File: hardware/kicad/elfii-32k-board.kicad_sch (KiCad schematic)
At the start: 15 parts, among them J1 ELFII_P3_86, U1 74HCT273, U2 62256, U3 74HCT04, U4 74HCT86, U5 74HCT32

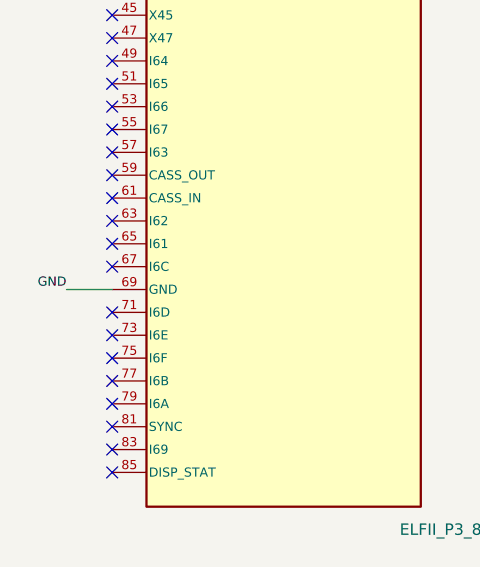
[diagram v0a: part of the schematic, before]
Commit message: Leave original-bus contact 69 NC pending GND discrepancy resolution
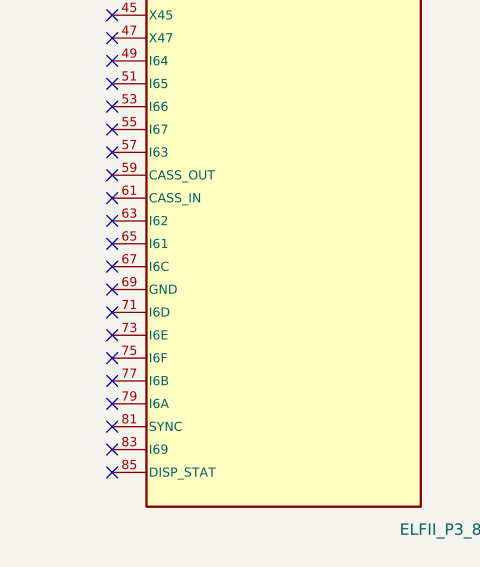
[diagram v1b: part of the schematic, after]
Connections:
- net GND: no longer J1.69 (GND)
- no-connect marks 70 -> 71
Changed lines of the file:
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@@
 (wire (pts (xy 56.950 243.740) (xy 51.870 243.740)) (stroke (width 0) (type default)))
 (label "GND" (at 51.870 243.740 0) (effects (font (size 1.016 1.016)) (justify right bottom)))
-(wire (pts (xy 56.950 325.020) (xy 51.870 325.020)) (stroke (width 0) (type default)))
-(label "GND" (at 51.870 325.020 0) (effects (font (size 1.016 1.016)) (justify right bottom)))
 (text "PROTOTYPE - NOT FABRICATION READY" (at 175 24 0) (effects (font (size 1.5 1.5)) (justify left)))
 (text "Original Netronics ELF II expansion bus - 86 contacts" (at 175 32 0) (effects (font (size 1.5 1.5)) (justify left)))
@@
 (no_connect (at 56.950 342.800))
 (no_connect (at 56.950 345.340))
+(no_connect (at 56.950 325.020))
 (sheet_instances (path "/" (page "1")))
 )

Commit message: Add functional schematic sections and explicit latch/decode annotations
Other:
- note added: "/CE = XOR(A15,REGION) OR NOT(ENABLE)"
- note added: "/OE = /CE OR /MRD /WE = /CE OR /MWR"
- note added: "32K STATIC RAM / U2"
- note added: "A0-A7: use MA0-MA7 during the memory phase"
- note added: "A8-A15: capture MA0-MA7 at TPA falling edge"
- note added: "CONTROL / 1802 CYCLES"
- note added: "EXPANSION BUS / J1"
- note added: "HIGH ADDRESS LATCH / U1"
- note added: "IMPORTANT: J1 pins 69 and 82 are disputed; remain NC."
- note added: "POWER BYPASS"
- note added: "REGION SELECT AND ENABLE"
- note added: "Schematic nets intentionally use short stubs and named labels."
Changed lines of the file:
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@@
 (no_connect (at 56.950 345.340))
 (no_connect (at 56.950 325.020))
+(text "EXPANSION BUS / J1" (at 41 40 0) (effects (font (size 1.8 1.8) (thickness 0.3)) (justify left)))
+(text "HIGH ADDRESS LATCH / U1" (at 175 75 0) (effects (font (size 1.8 1.8) (thickness 0.3)) (justify left)))
+(text "32K STATIC RAM / U2" (at 302 75 0) (effects (font (size 1.8 1.8) (thickness 0.3)) (justify left)))
+(text "CONTROL / 1802 CYCLES" (at 176 222 0) (effects (font (size 1.8 1.8) (thickness 0.3)) (justify left)))
+(text "REGION SELECT AND ENABLE" (at 305 319 0) (effects (font (size 1.8 1.8) (thickness 0.3)) (justify left)))
+(text "POWER BYPASS" (at 484 52 0) (effects (font (size 1.8 1.8) (thickness 0.3)) (justify left)))
+(text "A8-A15: capture MA0-MA7 at TPA falling edge" (at 176 157 0) (effects (font (size 1.27 1.27) (thickness 0.2)) (justify left)))
+(text "A0-A7: use MA0-MA7 during the memory phase" (at 176 165 0) (effects (font (size 1.27 1.27) (thickness 0.2)) (justify left)))
+(text "Schematic nets intentionally use short stubs and named labels." (at 176 173 0) (effects (font (size 1.27 1.27) (thickness 0.2)) (justify left)))
+(text "/CE = XOR(A15,REGION) OR NOT(ENABLE)" (at 314 222 0) (effects (font (size 1.27 1.27) (thickness 0.2)) (justify left)))
+(text "/OE = /CE OR /MRD      /WE = /CE OR /MWR" (at 314 230 0) (effects (font (size 1.27 1.27) (thickness 0.2)) (justify left)))
+(text "IMPORTANT: J1 pins 69 and 82 are disputed; remain NC." (at 176 181 0) (effects (font (size 1.27 1.27) (thickness 0.2)) (justify left)))
 (sheet_instances (path "/" (page "1")))
 )
